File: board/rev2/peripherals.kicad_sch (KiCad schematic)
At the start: 5 parts, among them J6 Micro_SD_Card_Det1, J7 Conn_01x09_Pin, SW1 SW_Push

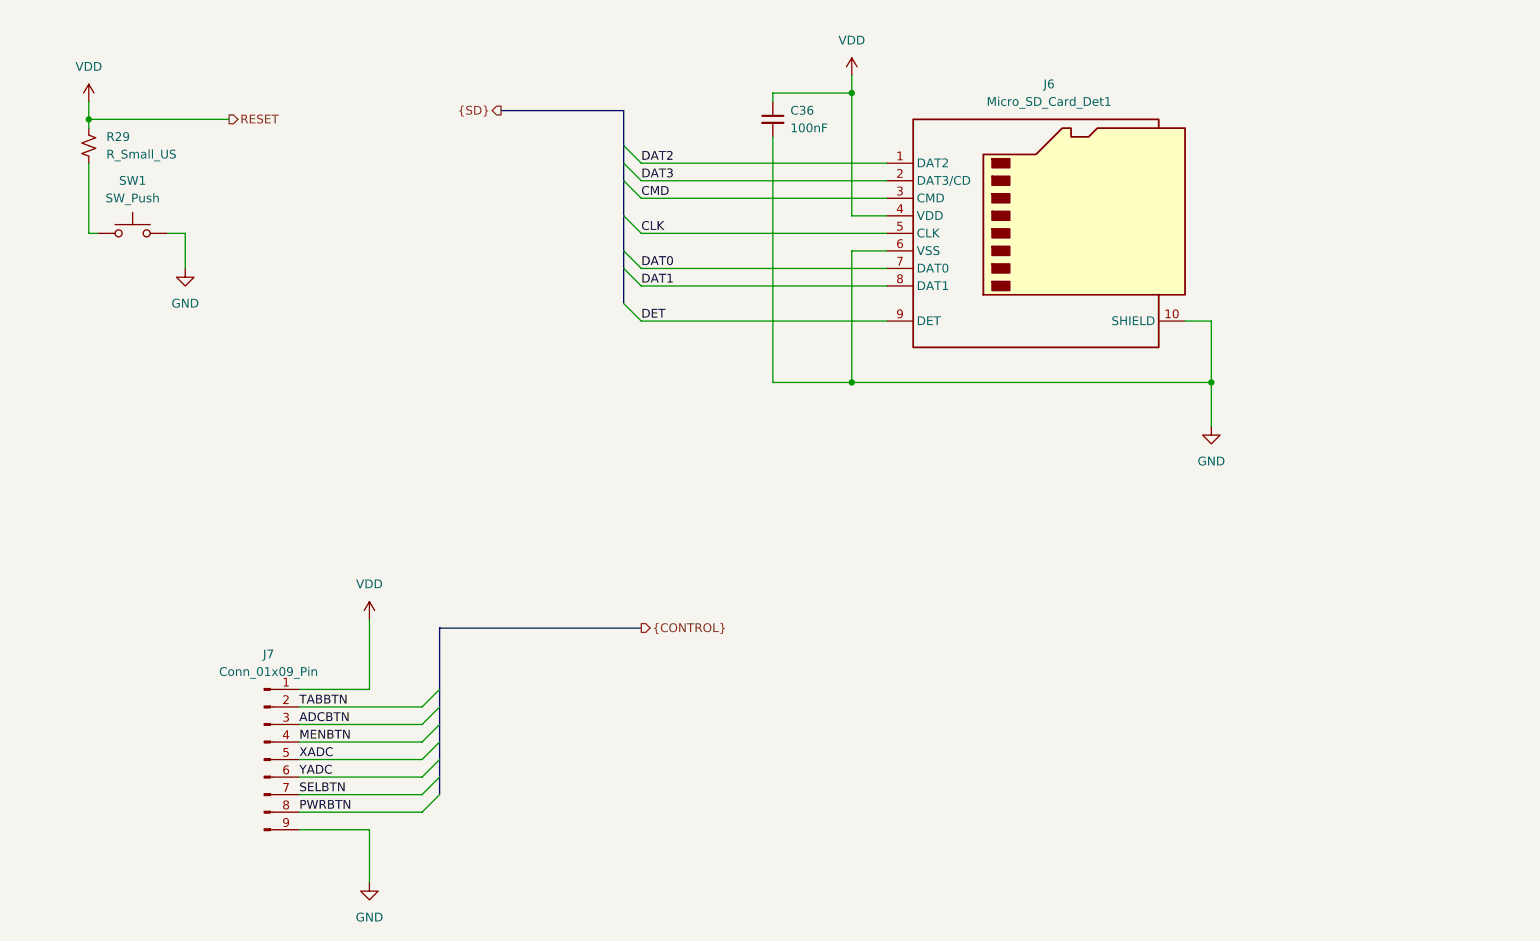
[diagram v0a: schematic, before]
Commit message: Board GPIO allocation
- and usbmux

still need to do termination on the big buses + a bunch of bypass caps
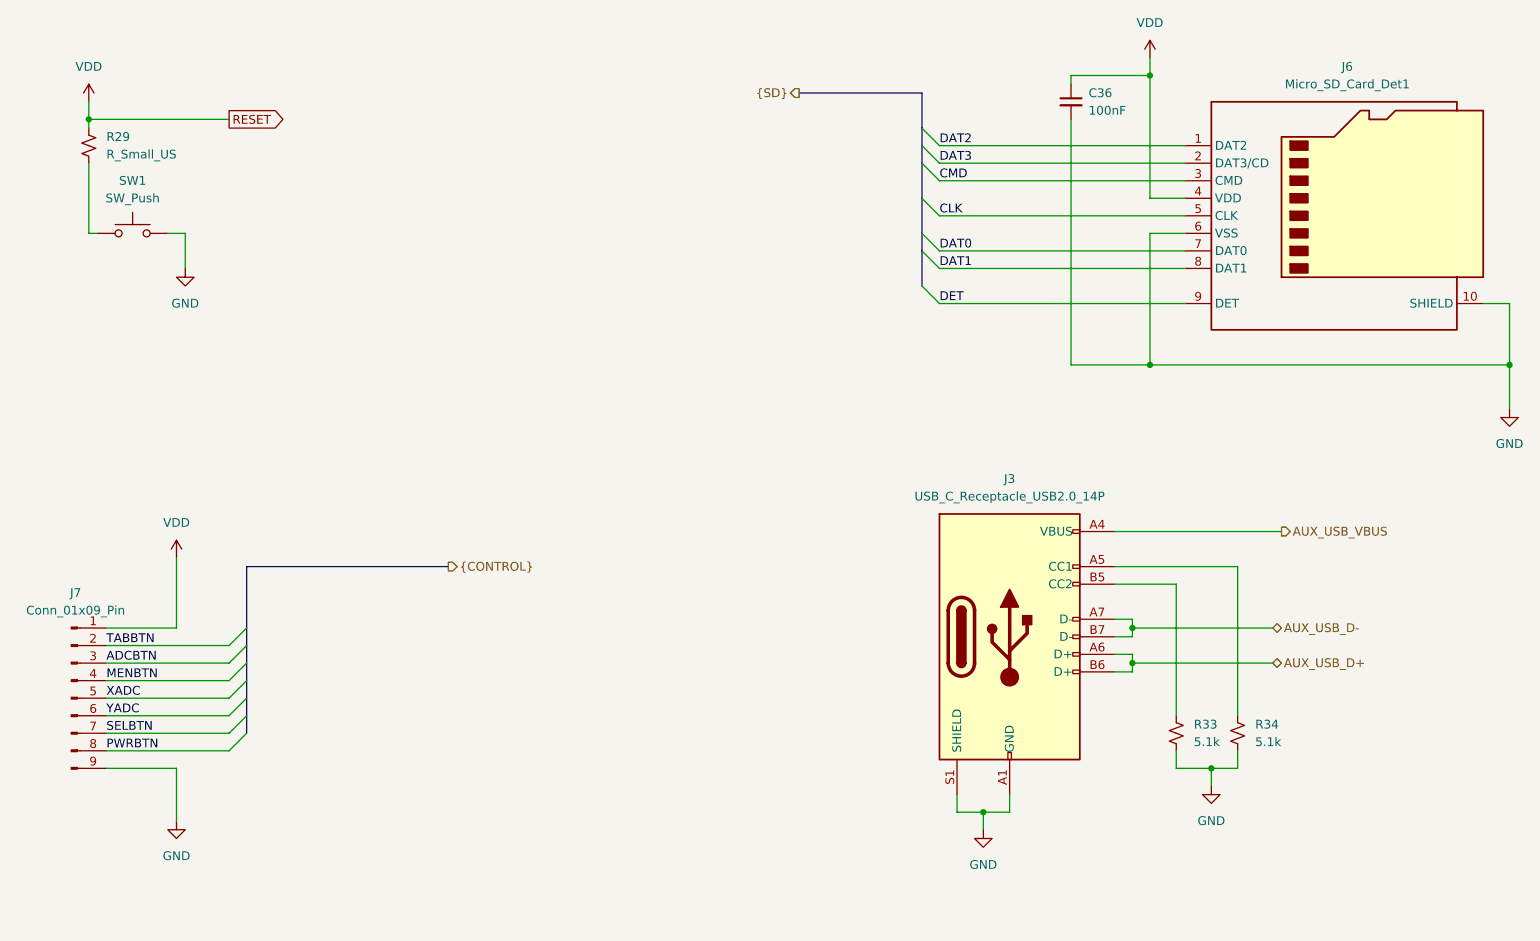
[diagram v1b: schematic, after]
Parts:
- added J3: USB_C_Receptacle_USB2.0_14P, symbol Connector:USB_C_Receptacle_USB2.0_14P
- added R33, R34: 5.1k, symbol Device:R_Small_US
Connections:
- net GND: now also J3.A1 (GND), J3.A12 (GND), J3.B1 (GND), J3.B12 (GND), J3.S1 (SHIELD), R33.2, R34.2
- new net: J3.A5 (CC1), R34.1
- new net: J3.B5 (CC2), R33.1
- new net AUX_USB_D+: J3.A6 (D+), J3.B6 (D+)
- new net AUX_USB_D-: J3.A7 (D-), J3.B7 (D-)
- new net AUX_USB_VBUS: J3.A4 (VBUS), J3.A9 (VBUS), J3.B4 (VBUS), J3.B9 (VBUS)
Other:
- company: (none) -> MLABS
- title: (none) -> Misc. External Connectors
- moved on the sheet: C36, J6, J7

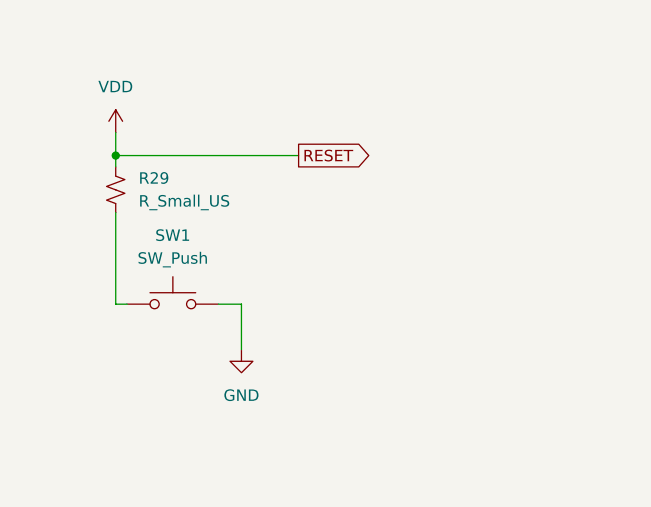
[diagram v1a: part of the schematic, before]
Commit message: Continue board, assign caps/res, adjust for JLC availability
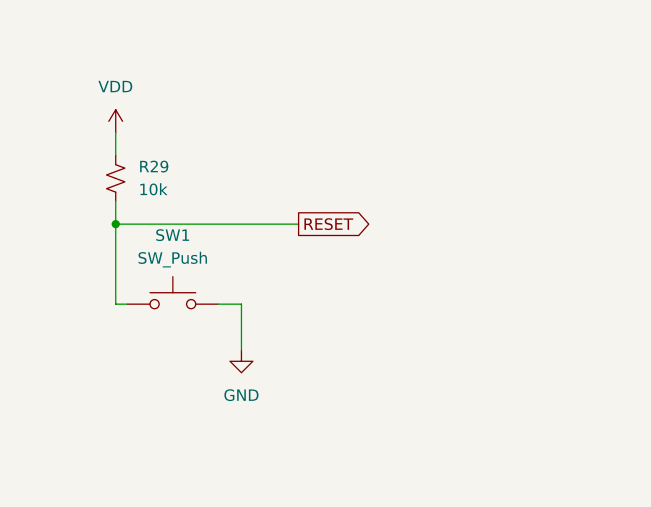
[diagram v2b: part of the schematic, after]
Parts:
- C36: footprint (none) -> Capacitor_SMD:C_0402_1005Metric; Part (none) -> CL05B104KB54PNC
- J7: footprint (none) -> Connector_PinHeader_2.54mm:PinHeader_1x09_P2.54mm_Horizontal
- R29: value R_Small_US -> 10k; footprint (none) -> Resistor_SMD:R_0805_2012Metric; Part (none) -> 0805W8F1002T5E
- R33, R34: footprint (none) -> Resistor_SMD:R_0603_1608Metric; Part (none) -> 0603WAF5101T5E
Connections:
- net RESET: now reaches R29.2, SW1.1
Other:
- moved on the sheet: R29
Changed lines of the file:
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@@
-	)
-	(junction
-		(at 50.8 45.72)
-		(diameter 0)
-		(color 0 0 0 0)
 	)
 	(junction
@@
 	)
 	(junction
+		(at 50.8 53.34)
+		(diameter 0)
+		(color 0 0 0 0)
+	)
+	(junction
 		(at 204.47 81.28)
 		(diameter 0)
@@
 	(wire
 		(pts
-			(xy 50.8 52.07) (xy 50.8 62.23)
+			(xy 50.8 50.8) (xy 50.8 53.34)
 		)
 		(stroke
@@
 	(wire
 		(pts
-			(xy 50.8 45.72) (xy 71.12 45.72)
-		)
-		(stroke
-			(width 0)
-			(type default)
-		)
-	)
-	(wire
-		(pts
 			(xy 199.39 110.49) (xy 217.17 110.49)
 		)
@@
 	(wire
 		(pts
+			(xy 50.8 53.34) (xy 50.8 62.23)
+		)
+		(stroke
+			(width 0)
+			(type default)
+		)
+	)
+	(wire
+		(pts
 			(xy 217.17 110.49) (xy 217.17 132.08)
 		)
@@
 	(wire
 		(pts
-			(xy 50.8 45.72) (xy 50.8 46.99)
+			(xy 50.8 43.18) (xy 50.8 45.72)
 		)
 		(stroke
@@
 		)
 	)
+	(wire
+		(pts
+			(xy 50.8 53.34) (xy 71.12 53.34)
+		)
+		(stroke
+			(width 0)
+			(type default)
+		)
+	)
 	(bus
 		(pts
@@
 		(pts
 			(xy 53.34 129.54) (xy 71.12 129.54)
-		)
-		(stroke
-			(width 0)
-			(type default)
-		)
-	)
-	(wire
-		(pts
-			(xy 50.8 43.18) (xy 50.8 45.72)
 		)
 		(stroke
@@
 	(global_label "RESET"
 		(shape output)
-		(at 71.12 45.72 0)
+		(at 71.12 53.34 0)
 		(fields_autoplaced yes)
 		(effects
@@
 		)
 		(property "Intersheetrefs" "${INTERSHEET_REFS}"
-			(at 79.8503 45.72 0)
+			(at 79.8503 53.34 0)
 			(effects
 				(font
@@
 			)
 		)
-		(property "Footprint" ""
+		(property "Footprint" "Resistor_SMD:R_0603_1608Metric"
 			(at 217.17 134.62 0)
 			(effects
@@
 		)
 		(property "Description" "Resistor, small US symbol"
+			(at 217.17 134.62 0)
+			(effects
+				(font
+					(size 1.27 1.27)
+				)
+				(hide yes)
+			)
+		)
+		(property "Part" "0603WAF5101T5E"
 			(at 217.17 134.62 0)
 			(effects
@@
 			)
 		)
-		(property "Footprint" ""
+		(property "Footprint" "Capacitor_SMD:C_0402_1005Metric"
 			(at 193.04 43.18 0)
 			(effects
@@
 		)
 		(property "Description" "Unpolarized capacitor, small symbol"
+			(at 193.04 43.18 0)
+			(effects
+				(font
+					(size 1.27 1.27)
+				)
+				(hide yes)
+			)
+		)
+		(property "Part" "CL05B104KB54PNC"
 			(at 193.04 43.18 0)
 			(effects
@@
 	(symbol
 		(lib_id "Device:R_Small_US")
-		(at 50.8 49.53 0)
+		(at 50.8 48.26 0)
 		(unit 1)
 		(exclude_from_sim no)
@@
 		(fields_autoplaced yes)
 		(property "Reference" "R29"
-			(at 53.34 48.2599 0)
+			(at 53.34 46.9899 0)
 			(effects
 				(font
@@
 			)
 		)
-		(property "Value" "R_Small_US"
-			(at 53.34 50.7999 0)
+		(property "Value" "10k"
+			(at 53.34 49.5299 0)
 			(effects
 				(font
@@
 			)
 		)
-		(property "Footprint" ""
-			(at 50.8 49.53 0)
+		(property "Footprint" "Resistor_SMD:R_0805_2012Metric"
+			(at 50.8 48.26 0)
 			(effects
 				(font
@@
 		)
 		(property "Datasheet" "~"
-			(at 50.8 49.53 0)
+			(at 50.8 48.26 0)
 			(effects
 				(font
@@
 		)
 		(property "Description" "Resistor, small US symbol"
-			(at 50.8 49.53 0)
+			(at 50.8 48.26 0)
+			(effects
+				(font
+					(size 1.27 1.27)
+				)
+				(hide yes)
+			)
+		)
+		(property "Part" "0805W8F1002T5E"
+			(at 50.8 48.26 0)
 			(effects
 				(font
@@
 			)
 		)
-		(property "Footprint" ""
+		(property "Footprint" "Resistor_SMD:R_0603_1608Metric"
 			(at 208.28 134.62 0)
 			(effects
@@
 		)
 		(property "Description" "Resistor, small US symbol"
+			(at 208.28 134.62 0)
+			(effects
+				(font
+					(size 1.27 1.27)
+				)
+				(hide yes)
+			)
+		)
+		(property "Part" "0603WAF5101T5E"
 			(at 208.28 134.62 0)
 			(effects
@@
 			)
 		)
-		(property "Footprint" ""
+		(property "Footprint" "Connector_PinHeader_2.54mm:PinHeader_1x09_P2.54mm_Horizontal"
 			(at 48.26 129.54 0)
 			(effects
